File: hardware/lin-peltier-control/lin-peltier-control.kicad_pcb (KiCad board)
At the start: 4 copper layers, 55.6 x 43.2 mm, 58 parts, among them J1 UPDI, J2 I2C LCD, J3 LINBus, J4 PELTIER, Q1 2N7002, Q2 2N7002, Q3 2N7002, Q4 SUD50P04-08, U1 TJA1021T, U2 ATtiny824-X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

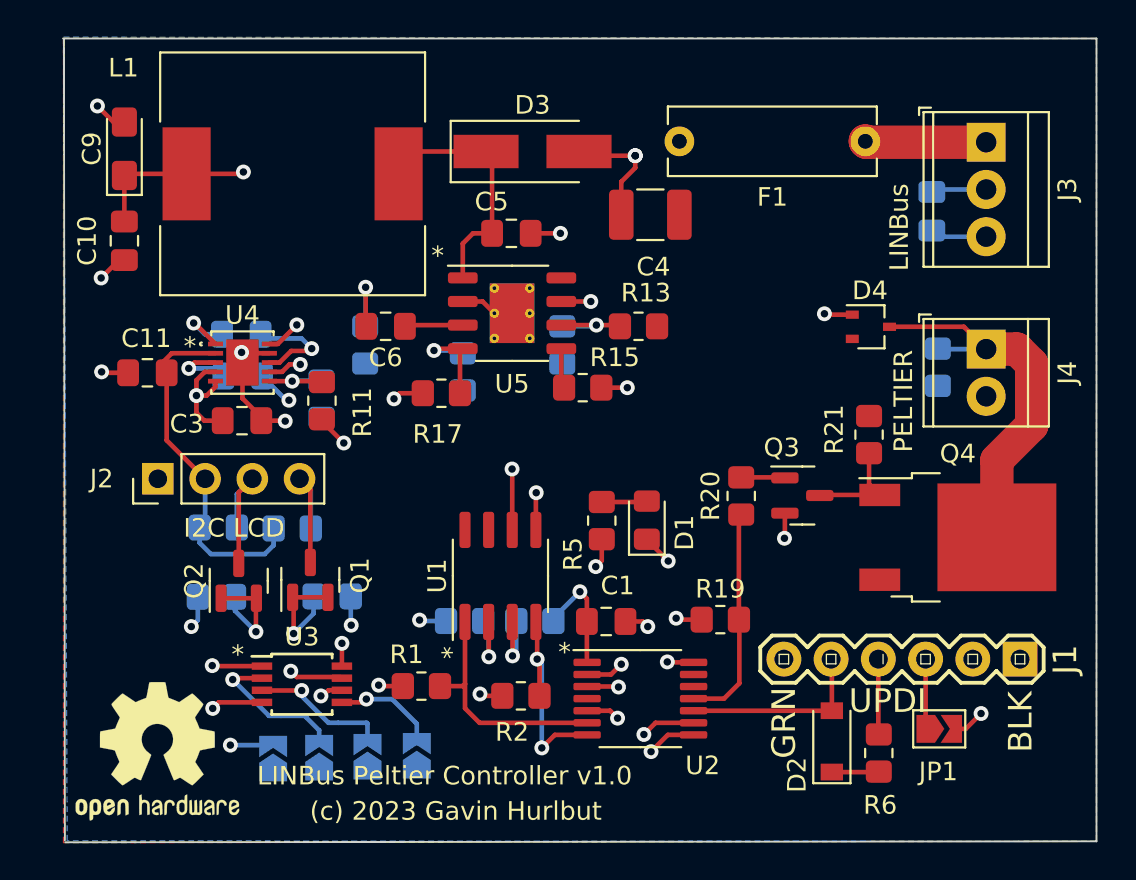
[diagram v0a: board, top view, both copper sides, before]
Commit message: Update the peltier controller to include INA219.
- resistor value to be changed in a bit.
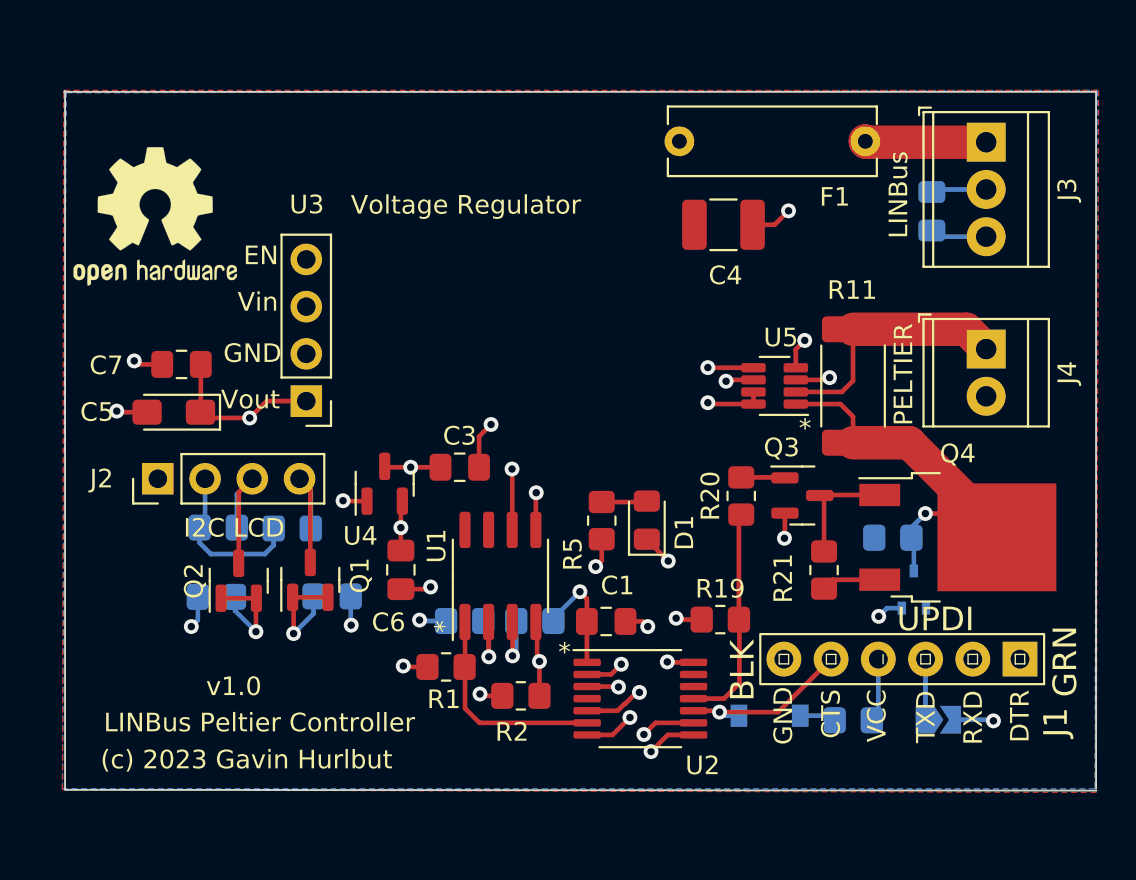
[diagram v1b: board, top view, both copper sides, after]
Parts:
- removed C10, C11: 10uF, Capacitor_SMD:C_0805_2012Metric_Pad1.18x1.45mm_HandSolder
- removed C8: 2.2uF, Capacitor_SMD:C_0805_2012Metric_Pad1.18x1.45mm_HandSolder
- removed C9: 100uF Ta 6V, Capacitor_Tantalum_SMD:CP_EIA-3216-10_Kemet-I_Pad1.58x1.35mm_HandSolder
- removed D3: BYS10-35, Diode_SMD:D_SMA_Handsoldering
- removed JP2: A3, Jumper:SolderJumper-2_P1.3mm_Open_TrianglePad1.0x1.5mm
- removed JP3: A2, Jumper:SolderJumper-2_P1.3mm_Open_TrianglePad1.0x1.5mm
- removed JP4: A1, Jumper:SolderJumper-2_P1.3mm_Open_TrianglePad1.0x1.5mm
- removed JP5: A0, Jumper:SolderJumper-2_P1.3mm_Open_TrianglePad1.0x1.5mm
- removed L1: 33uH 5A 88mOhm, Beirdo:PM4346.333NLT
- removed R12: 100k 1%, Resistor_SMD:R_0805_2012Metric_Pad1.20x1.40mm_HandSolder
- removed R13: 909k 1%, Resistor_SMD:R_0805_2012Metric_Pad1.20x1.40mm_HandSolder
- removed R14: 324k 1%, Resistor_SMD:R_0805_2012Metric_Pad1.20x1.40mm_HandSolder
- removed R15: 47k, Resistor_SMD:R_0805_2012Metric_Pad1.20x1.40mm_HandSolder
- removed R16: 6k2, Resistor_SMD:R_0805_2012Metric_Pad1.20x1.40mm_HandSolder
- removed R17: 1k3, Resistor_SMD:R_0805_2012Metric_Pad1.20x1.40mm_HandSolder
- removed R18: 560R, Resistor_SMD:R_0805_2012Metric_Pad1.20x1.40mm_HandSolder
- C3: value 2.2uF -> 1uF
- C5: value 100nF -> 100uF Ta 6V; footprint Capacitor_SMD:C_0805_2012Metric_Pad1.18x1.45mm_HandSolder -> Capacitor_Tantalum_SMD:CP_EIA-3216-10_Kemet-I_Pad1.58x1.35mm_HandSolder
- C6: value 10nF -> 1uF
- C7: value 2.2uF -> 10uF; moved to F.Cu
- D2, D4, JP1, R6: moved to B.Cu
- J1: footprint Beirdo:FTDI_BASIC -> Beirdo:FTDI-TARGET
- R11: value 357k 1% -> 100m 1% 2W; footprint Resistor_SMD:R_0805_2012Metric_Pad1.20x1.40mm_HandSolder -> Resistor_SMD:R_2512_6332Metric_Pad1.40x3.35mm_HandSolder
- U3: value PCA9536DP -> Voltage Regulator; footprint Package_SO:TSSOP-8_3x3mm_P0.65mm -> Beirdo:Switching_Regulator_Module
- U4: value LTC3203BEDD-PBF -> MCP1754S-3302xCB; footprint UltraLibrarian:LTC3203BEDD-PBF -> Package_TO_SOT_SMD:SOT-23
- U5: value BD9G341EFJ -> INA219BxDCN; footprint Package_SO:HTSOP-8-1EP_3.9x4.9mm_P1.27mm_EP2.4x3.2mm_ThermalVias -> Package_TO_SOT_SMD:SOT-23-8
- moved REF** 28.8 mm to (180.0, 68.0)
- moved R11 28.6 mm to (217.5, 77.1), turned to -90 degrees
- moved C5 20.5 mm to (181.0, 78.5)
- moved U3 15.1 mm to (188.2, 78.0), turned to 180 degrees
- moved U5 14.7 mm to (213.3, 77.1), turned to 180 degrees
- moved D4 14.3 mm to (220.8, 88.1), turned to 90 degrees
- moved C6 13.1 mm to (193.2, 87.0), turned to -90 degrees
- moved C3 12.0 mm to (196.4, 81.5)
- moved U4 10.0 mm to (192.3, 82.4), turned to 90 degrees
- moved R22 9.48 mm to (219.7, 85.3), turned to 180 degrees
- moved R21 7.68 mm to (216.0, 87.0), turned to 90 degrees
- moved C4 3.97 mm to (210.6, 68.4), turned to 0 degrees
- moved D2 3.63 mm to (213.1, 94.8), turned to 180 degrees
- moved C7 3.35 mm to (181.4, 76.0)
- moved R6 2.23 mm to (217.6, 95.1), turned to 0 degrees
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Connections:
- C3 pad 1: +3V3 -> +5V
- C5 pad 1: Net-(C5-Pad1) -> +5V
- C5 pad 2: Net-(C5-Pad2) -> GND
- C6 pad 1: Net-(C6-Pad1) -> +3V3
- C6 pad 2: Net-(C6-Pad2) -> GND
- C7 pad 1: Net-(C7-Pad1) -> +5V
- C7 pad 2: Net-(C7-Pad2) -> GND
- D4 pad 3: PELTIER+ -> Net-(D4-Pad3)
- Q1 pad 1: SCL3V -> SCL
- Q1 pad 2: SCL3V -> SCL
- Q2 pad 1: SDA3V -> SDA
- Q2 pad 2: SDA3V -> SDA
- Q4 pad 2: PELTIER+ -> Net-(D4-Pad3)
- R10 pad 2: SCL3V -> SCL
- R11 pad 1: +3V3 -> PELTIER+
- R11 pad 2: Net-(R11-Pad2) -> Net-(D4-Pad3)
- R22 pad 1: PELTIER+ -> Net-(D4-Pad3)
- R9 pad 2: SDA3V -> SDA
- U2 pad 8: SDA3V -> SDA
- U2 pad 9: SCL3V -> SCL
- U3 pad 1: Net-(JP5-Pad2) -> +5V
- U3 pad 2: Net-(JP4-Pad2) -> GND
- U3 pad 3: Net-(JP3-Pad2) -> +12V
- U3 pad 4: GND -> unconnected-(U3-Pad4)
- U4 pad 1: Net-(C8-Pad1) -> GND
- U4 pad 2: +5V -> +3V3
- U4 pad 3: Net-(C7-Pad2) -> +5V
- U5 pad 1: Net-(C5-Pad2) -> Net-(D4-Pad3)
- U5 pad 2: GND -> PELTIER+
- U5 pad 3: Net-(C6-Pad1) -> GND
- U5 pad 4: Net-(R17-Pad2) -> +3V3
- U5 pad 5: Net-(R15-Pad1) -> SCL
- U5 pad 6: Net-(R13-Pad2) -> SDA
- U5 pad 7: Net-(C5-Pad1) -> SCL
- U5 pad 8: +12V -> SCL
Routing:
- net SCL: track 0.00 -> 57.1 mm, vias 0 -> 4
- net SDA: track 0.00 -> 55.8 mm, vias 0 -> 3
- net SDA3V: track 37.3 -> 0.00 mm, vias 3 -> 0
- net SCL3V: track 32.8 -> 0.00 mm, vias 3 -> 0
- net Net-(D4-Pad3): track 0.00 -> 22.7 mm, vias 0 -> 1
- net +3V3: track 38.2 -> 21.5 mm, vias 14 -> 10
- net Net-(C5-Pad2): track 13.4 -> 0.00 mm
- net GND: track 37.0 -> 23.6 mm, vias 15 -> 12
- net Net-(JP5-Pad2): track 9.66 -> 0.00 mm, vias 2 -> 0
- net Net-(C7-Pad1): track 8.57 -> 0.00 mm, vias 2 -> 0
- net Net-(JP4-Pad2): track 8.13 -> 0.00 mm, vias 1 -> 0
- net Net-(JP3-Pad2): track 7.65 -> 0.00 mm, vias 1 -> 0
- net Net-(C5-Pad1): track 7.53 -> 0.00 mm, vias 2 -> 0
- net PELTIER+: track 21.2 -> 13.7 mm
- net Net-(C8-Pad2): track 5.66 -> 0.00 mm, vias 1 -> 0
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- added copper zone on In1.Cu, net +5V
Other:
- board size 55.6 x 43.2 mm -> 55.5 x 37.6 mm
- board text added: "LINBus Peltier Controller"
- board text added: "v1.0"
- board text removed: "LINBus Peltier Controller v1.0"

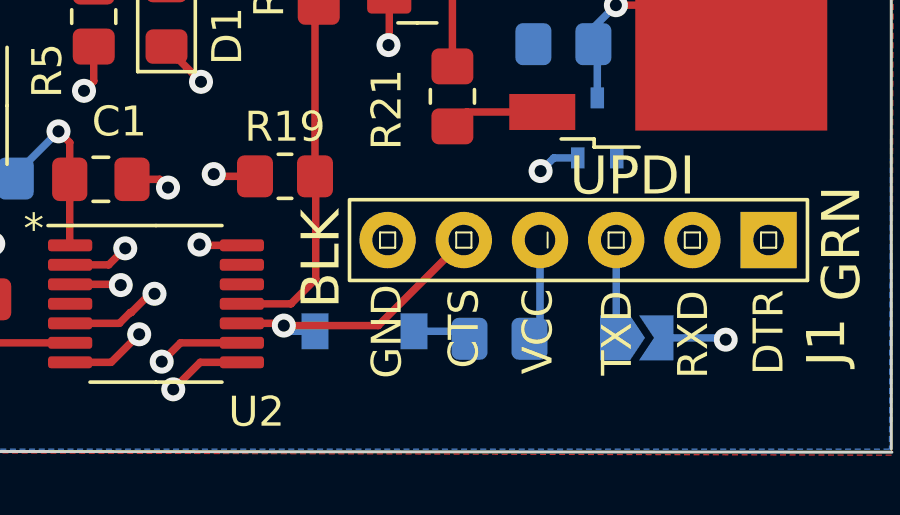
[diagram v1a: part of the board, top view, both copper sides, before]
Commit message: Update the schematics... remove PCA9536, use voltage regulator
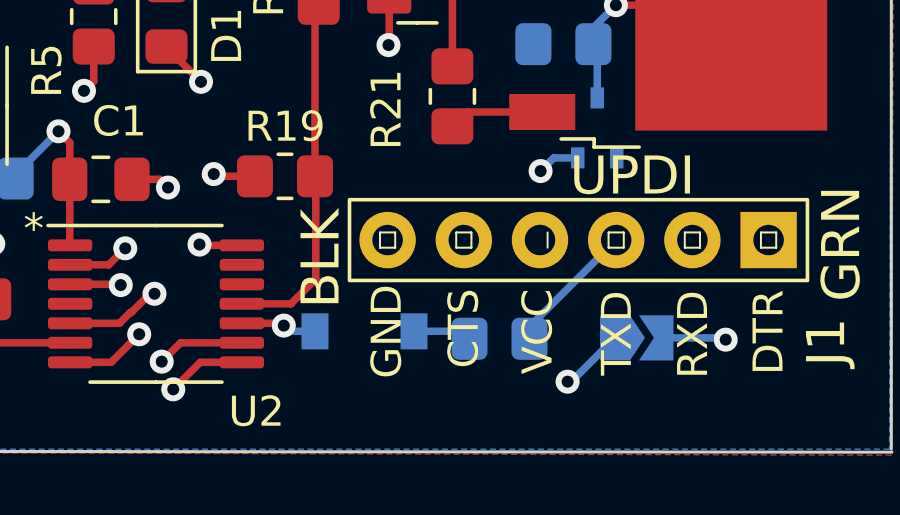
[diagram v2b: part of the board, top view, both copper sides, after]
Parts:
- R11: value 100m 1% 2W -> 22m 1% 5W
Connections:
- J1 pad 1: GND -> unconnected-(J1-Pad1)
- J1 pad 2: unconnected-(J1-Pad2) -> UPDI
- J1 pad 3: Net-(J1-Pad3) -> Net-(R6-Pad2)
- J1 pad 4: Net-(J1-Pad4) -> Net-(JP1-Pad1)
- J1 pad 5: UPDI -> unconnected-(J1-Pad5)
- J1 pad 6: unconnected-(J1-Pad6) -> GND
- JP1 pad 1: Net-(J1-Pad3) -> Net-(JP1-Pad1)
- R6 pad 2: Net-(J1-Pad4) -> Net-(R6-Pad2)
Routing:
- net UPDI: track 9.78 -> 17.3 mm
- net Net-(JP1-Pad1): track 0.00 -> 7.34 mm, vias 0 -> 1
- net Net-(R6-Pad2): track 0.00 -> 4.98 mm
- net Net-(J1-Pad4): track 3.43 -> 0.00 mm
- net Net-(J1-Pad3): track 3.28 -> 0.00 mm
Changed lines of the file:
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@@
   (net 13 "UPDI")
   (net 14 "+BATT")
-  (net 15 "unconnected-(J1-Pad2)")
-  (net 16 "Net-(J1-Pad3)")
+  (net 15 "unconnected-(J1-Pad1)")
+  (net 16 "Net-(R6-Pad2)")
   (net 17 "+3V3")
   (net 18 "SCL5V")
   (net 19 "SDA5V")
-  (net 20 "Net-(J1-Pad4)")
-  (net 21 "unconnected-(J1-Pad6)")
+  (net 20 "Net-(JP1-Pad1)")
+  (net 21 "unconnected-(J1-Pad5)")
   (net 22 "Net-(R5-Pad1)")
   (net 23 "Net-(D1-Pad2)")
@@
       (effects (font (size 1 1) (thickness 0.15)))
     )
-    (fp_text value "100m 1% 2W" (at 0 2.62 90) (layer "F.Fab")
+    (fp_text value "22m 1% 5W" (at 0 2.62 90) (layer "F.Fab")
       (effects (font (size 1 1) (thickness 0.15)))
     )
@@
     (property "Sheetfile" "lin-peltier-control.kicad_sch")
     (property "Sheetname" "")
-    (attr exclude_from_pos_files exclude_from_bom)
+    (attr exclude_from_pos_files)
     (fp_text reference "J1" (at -1.93 -3.4 270) (layer "F.SilkS")
       (effects (font (size 1.27 1.27) (thickness 0.127)))
@@
     (fp_rect (start -1.2954 -1.3462) (end 13.97 1.3462) (layer "F.SilkS") (width 0.12) (fill none))
     (pad "1" thru_hole rect (at 0 0 180) (size 1.8796 1.8796) (drill 1.016) (layers *.Cu *.Paste *.Mask)
-      (net 1 "GND") (pinfunction "GND") (pintype "passive"))
+      (net 15 "unconnected-(J1-Pad1)") (pinfunction "DTR") (pintype "passive+no_connect"))
     (pad "2" thru_hole circle (at 2.54 0 180) (size 1.8796 1.8796) (drill 1.016) (layers *.Cu *.Paste *.Mask)
-      (net 15 "unconnected-(J1-Pad2)") (pinfunction "CTS") (pintype "passive+no_connect"))
+      (net 13 "UPDI") (pinfunction "RXD") (pintype "passive"))
     (pad "3" thru_hole circle (at 5.08 0 180) (size 1.8796 1.8796) (drill 1.016) (layers *.Cu *.Paste *.Mask)
-      (net 16 "Net-(J1-Pad3)") (pinfunction "VCC") (pintype "passive"))
+      (net 16 "Net-(R6-Pad2)") (pinfunction "TXD") (pintype "passive"))
     (pad "4" thru_hole circle (at 7.62 0 180) (size 1.8796 1.8796) (drill 1.016) (layers *.Cu *.Paste *.Mask)
-      (net 20 "Net-(J1-Pad4)") (pinfunction "TXD") (pintype "passive"))
+      (net 20 "Net-(JP1-Pad1)") (pinfunction "VCC") (pintype "passive"))
     (pad "5" thru_hole circle (at 10.16 0 180) (size 1.8796 1.8796) (drill 1.016) (layers *.Cu *.Paste *.Mask)
-      (net 13 "UPDI") (pinfunction "RXD") (pintype "passive"))
+      (net 21 "unconnected-(J1-Pad5)") (pinfunction "CTS") (pintype "passive+no_connect"))
     (pad "6" thru_hole circle (at 12.7 0 180) (size 1.8796 1.8796) (drill 1.016) (layers *.Cu *.Paste *.Mask)
-      (net 21 "unconnected-(J1-Pad6)") (pinfunction "RTS") (pintype "passive+no_connect"))
+      (net 1 "GND") (pinfunction "GND") (pintype "passive"))
   )
   (footprint "Resistor_SMD:R_0805_2012Metric_Pad1.20x1.40mm_HandSolder" (layer "B.Cu")
@@
       (net 24 "Net-(D2-Pad1)") (pintype "passive"))
     (pad "2" smd roundrect (at 1 0) (size 1.2 1.4) (layers "B.Cu" "B.Paste" "B.Mask") (roundrect_rratio 0.2083333333)
-      (net 20 "Net-(J1-Pad4)") (pintype "passive"))
+      (net 16 "Net-(R6-Pad2)") (pintype "passive"))
     (model "${KICAD6_3DMODEL_DIR}/Resistor_SMD.3dshapes/R_0805_2012Metric.wrl"
       (offset (xyz 0 0 0))
@@
     (fp_line (start -1.65 1.25) (end 1.65 1.25) (layer "B.CrtYd") (width 0.05))
     (pad "1" smd custom (at -0.725 0) (size 0.3 0.3) (layers "B.Cu" "B.Mask")
-      (net 16 "Net-(J1-Pad3)") (pinfunction "A") (pintype "passive") (zone_connect 2)
+      (net 20 "Net-(JP1-Pad1)") (pinfunction "A") (pintype "passive") (zone_connect 2)
       (options (clearance outline) (anchor rect))
       (primitives
@@
   (segment (start 220.16 89.06) (end 219.36 89.06) (width 0.25) (layer "B.Cu") (net 12))
   (segment (start 210.36 94.65) (end 210.285 94.575) (width 0.25) (layer "F.Cu") (net 13))
-  (segment (start 216.4 91.84) (end 216.36 91.8) (width 0.25) (layer "F.Cu") (net 13))
-  (segment (start 213.51 94.65) (end 210.36 94.65) (width 0.25) (layer "F.Cu") (net 13))
-  (segment (start 216.36 91.8) (end 213.51 94.65) (width 0.25) (layer "F.Cu") (net 13))
   (segment (start 210.285 94.575) (end 208.9625 94.575) (width 0.25) (layer "F.Cu") (net 13))
   (via (at 210.36 94.65) (size 0.8) (drill 0.4) (layers "F.Cu" "B.Cu") (net 13))
+  (segment (start 223.98 91.8) (end 221.13 94.65) (width 0.25) (layer "In1.Cu") (net 13))
+  (segment (start 221.13 94.65) (end 210.36 94.65) (width 0.25) (layer "In1.Cu") (net 13))
   (segment (start 210.55 94.84) (end 210.36 94.65) (width 0.25) (layer "B.Cu") (net 13))
   (segment (start 211.4 94.84) (end 210.55 94.84) (width 0.25) (layer "B.Cu") (net 13))
@@
   (segment (start 224.7 64) (end 218.25 64) (width 1.8) (layer "F.Cu") (net 14))
   (segment (start 218.275 64) (end 218.2 63.925) (width 0.25) (layer "F.Cu") (net 14))
-  (segment (start 221.4 95.06) (end 221.44 95.02) (width 0.25) (layer "B.Cu") (net 16))
-  (segment (start 221.44 95.02) (end 221.44 91.8) (width 0.25) (layer "B.Cu") (net 16))
+  (segment (start 218.55 95.09) (end 218.55 94.69) (width 0.25) (layer "B.Cu") (net 16))
+  (segment (start 218.55 94.69) (end 221.44 91.8) (width 0.25) (layer "B.Cu") (net 16))
+  (segment (start 218.55 95.09) (end 218.9 94.74) (width 0.25) (layer "B.Cu") (net 16))
   (segment (start 198.675 93.775) (end 197.575 93.775) (width 0.25) (layer "F.Cu") (net 17))
   (segment (start 203.225 89.775) (end 203.225 91.9375) (width 0.25) (layer "F.Cu") (net 17))
@@
   (segment (start 184.4 84.725) (end 184.4 82.93) (width 0.25) (layer "B.Cu") (net 19))
   (segment (start 184.4 82.93) (end 185.23 82.1) (width 0.25) (layer "B.Cu") (net 19))
-  (segment (start 218.9 94.74) (end 218.9 91.8) (width 0.25) (layer "B.Cu") (net 20))
-  (segment (start 218.55 95.09) (end 218.9 94.74) (width 0.25) (layer "B.Cu") (net 20))
+  (via (at 219.82 96.52) (size 0.8) (drill 0.4) (layers "F.Cu" "B.Cu") (net 20))
+  (segment (start 218.9 95.6) (end 219.82 96.52) (width 0.25) (layer "In2.Cu") (net 20))
+  (segment (start 218.9 91.8) (end 218.9 95.6) (width 0.25) (layer "In2.Cu") (net 20))
+  (segment (start 221.4 95.06) (end 221.44 95.02) (width 0.25) (layer "B.Cu") (net 20))
+  (segment (start 219.82 96.52) (end 219.94 96.52) (width 0.25) (layer "B.Cu") (net 20))
+  (segment (start 219.94 96.52) (end 221.4 95.06) (width 0.25) (layer "B.Cu") (net 20))
+  (segment (start 216.4 91.84) (end 216.36 91.8) (width 0.25) (layer "F.Cu") (net 21))
   (segment (start 203.2375 94.575) (end 204.879695 94.575) (width 0.25) (layer "F.Cu") (net 22))
   (segment (start 204.025 86.5) (end 203.7 86.825) (width 0.25) (layer "F.Cu") (net 22))
